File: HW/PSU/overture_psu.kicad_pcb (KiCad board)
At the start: 2 copper layers, 100 x 50 mm, 16 parts, among them J1 OUT, J2 IN, J3 LED

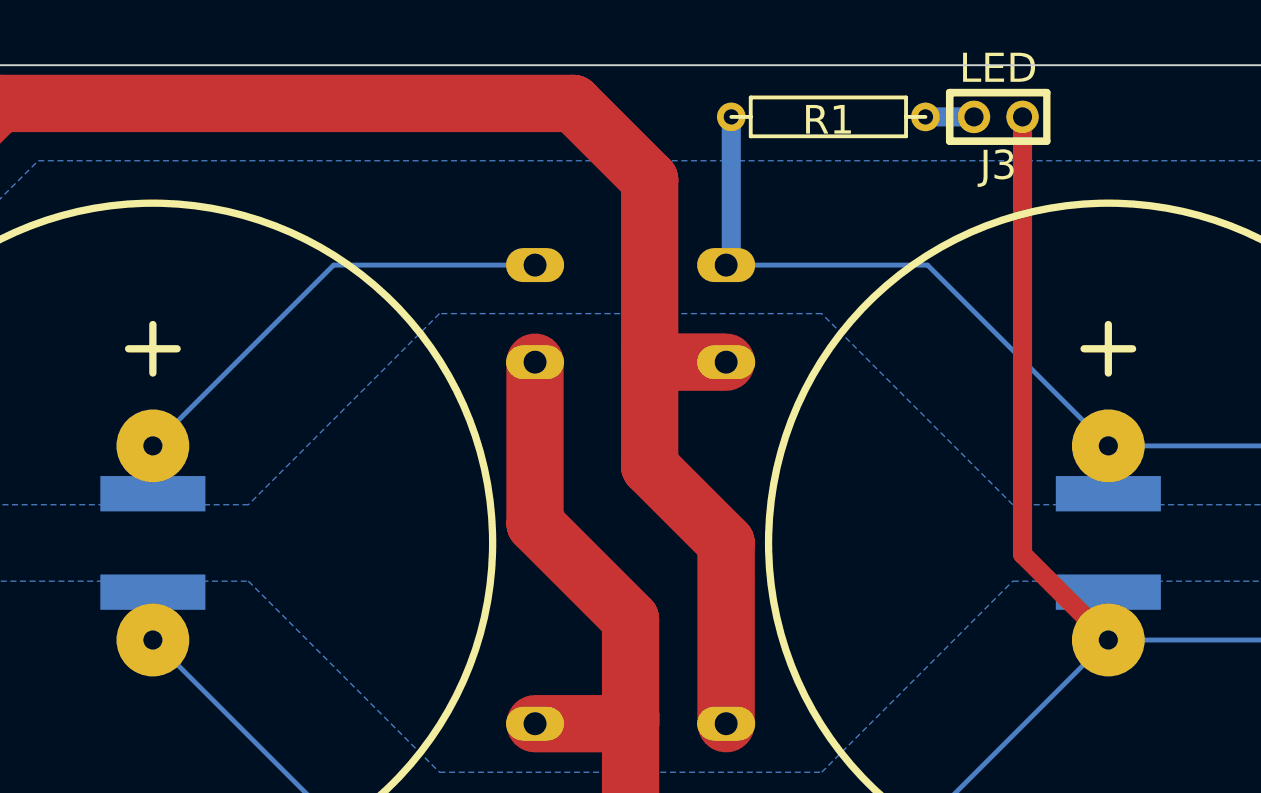
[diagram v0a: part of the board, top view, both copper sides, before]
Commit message: Updated to new KiCAD, Capacitor hole size corrected.
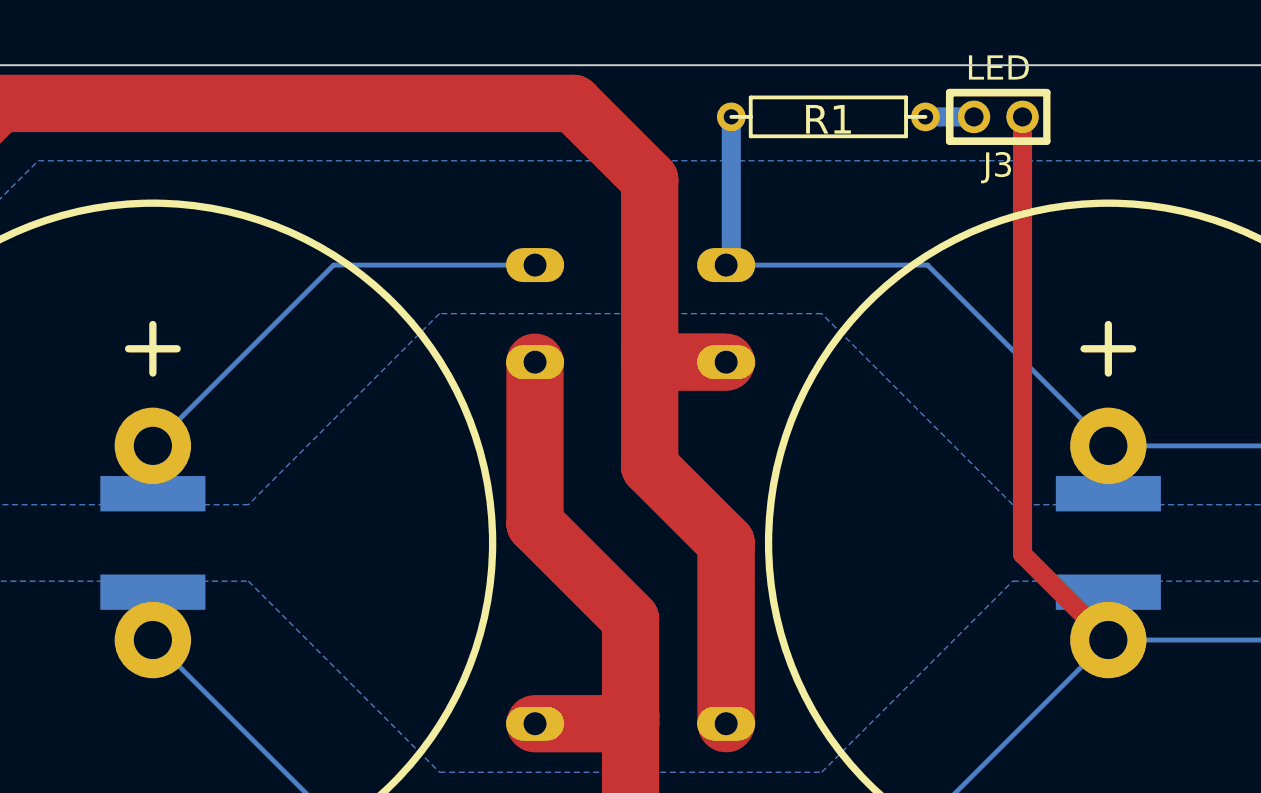
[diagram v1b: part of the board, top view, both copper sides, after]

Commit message: Add V3 (Actually built)
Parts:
- removed MNT_HOLE_3.5 (x4): , MNT_HOLE_3.5
- added C5: 10000uF/50V, Capacitors_ThroughHole:CP_Radial_D35.0mm_P10.00mm_SnapIn, F.Cu at (108.0, 57.0)
- added C6: 10000uF/50V, Capacitors_ThroughHole:CP_Radial_D35.0mm_P10.00mm_SnapIn, F.Cu at (144.0, 57.0)
- added C7: 1uF/250V, Capacitors_ThroughHole:C_Rect_L26.5mm_W11.5mm_P22.50mm_MKS4, F.Cu at (124.5, 32.0)
- added C8: 1uF/250V, Capacitors_ThroughHole:C_Rect_L26.5mm_W11.5mm_P22.50mm_MKS4, F.Cu at (154.5, 32.0)
- added J4: OUT2, suf_connector_ncw:CONN_NCW396-03S, F.Cu at (28.0, 77.0)
- added J5: Protect, Connectors_JST:JST_EH_B03B-EH-A_03x2.50mm_Straight, F.Cu at (150.6, 81.2)
- added MNT_HOLE_3.5S: Val**, suf_mounting:MNT_HOLE_3.5S, F.Cu at (141.0, 96.0)
- added MNT_HOLE_3.5S: Val**, suf_mounting:MNT_HOLE_3.5S, F.Cu at (49.0, 96.0)
- added MNT_HOLE_3.5S: Val**, suf_mounting:MNT_HOLE_3.5S, F.Cu at (165.0, 25.0)
- added MNT_HOLE_3.5S: Val**, suf_mounting:MNT_HOLE_3.5S, F.Cu at (25.0, 25.0)
- added REF**: sink60x100, suf_heatsink:sink60x100, F.Cu at (95.0, 90.0)
- C1: footprint C4P_D14 -> Capacitors_ThroughHole:CP_Radial_D35.0mm_P10.00mm_SnapIn
- C2: value 100nF/50V -> 10000uF/50V; footprint c_2220 -> Capacitors_ThroughHole:CP_Radial_D35.0mm_P10.00mm_SnapIn; moved to F.Cu
- C3: value 100nF/50V -> 1uF/250V; footprint c_2220 -> Capacitors_ThroughHole:C_Rect_L26.5mm_W11.5mm_P22.50mm_MKS4; moved to F.Cu
- C4: value 10000uF/50V -> 1uF/250V; footprint C4P_D14 -> Capacitors_ThroughHole:C_Rect_L26.5mm_W11.5mm_P22.50mm_MKS4
- D1, D2, D3, D4: footprint TO220-2 -> TO_SOT_Packages_THT:TO-220-2_Vertical; moved to F.Cu
- J1: value OUT -> OUT1; footprint CONN_NCW396-02R -> suf_connector_ncw:CONN_NCW396-03S
- J2: footprint CONN_NCW396-02R -> Terminal_Blocks:TerminalBlock_bornier-4_P5.08mm; moved to B.Cu
- J3: footprint HDR-2 -> suf_connector_ncw:CONN_NCW254-02S
- R1: footprint R4 -> Resistors_ThroughHole:R_Axial_DIN0207_L6.3mm_D2.5mm_P10.16mm_Horizontal
- moved C3 223.8 mm to (58.0, 32.0), turned to 180 degrees
- moved J3 207.6 mm to (39.0, 78.0)
- moved C4 199.4 mm to (88.0, 32.0), turned to 180 degrees
- moved R1 195.2 mm to (43.0, 78.0)
- moved C1 186.8 mm to (36.0, 57.0), turned to 0 degrees
- moved D1 162.5 mm to (62.5, 87.0)
- moved D3 157.8 mm to (77.5, 87.0)
- moved C2 157.3 mm to (72.0, 57.0), turned to 0 degrees
- moved J1 130.0 mm to (162.0, 77.0), turned to 0 degrees
- moved D2 126.1 mm to (117.5, 87.0)
- moved D4 122.3 mm to (132.5, 87.0)
- moved J2 104.4 mm to (102.5, 78.0), turned to 180 degrees
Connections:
- C1 pad 1: N-000001 -> Net-(C1-Pad1)
- C1 pad 2: N-000005 -> GND
- C2 pad 1: N-000001 -> GND
- C2 pad 2: N-000005 -> Net-(C2-Pad2)
- C3 pad 1: N-000001 -> GND
- C3 pad 2: N-000005 -> Net-(C1-Pad1)
- C4 pad 1: N-000001 -> Net-(C2-Pad2)
- C4 pad 2: N-000005 -> GND
- D1 pad 1: N-000001 -> Net-(C1-Pad1)
- D2 pad 1: N-000002 -> Net-(D2-Pad1)
- D3 pad 1: N-000001 -> Net-(C1-Pad1)
- D4 pad 1: N-000003 -> Net-(D1-Pad2)
- J1 pad 1: N-000001 -> Net-(C1-Pad1)
- J1 pad 2: N-000005 -> GND
- J2 pad 1: N-000002 -> Net-(D2-Pad1)
- J2 pad 2: N-000003 -> GND
- J3 pad 1: N-000005 -> Net-(J3-Pad1)
- J3 pad 2: N-000004 -> GND
- R1 pad 1: N-000001 -> Net-(J3-Pad1)
- R1 pad 2: N-000004 -> Net-(C1-Pad1)
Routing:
- net GND: track 0.00 -> 326.8 mm
- net Net-(C1-Pad1): track 0.00 -> 299.1 mm
- net Net-(C2-Pad2): track 0.00 -> 281.9 mm
- net N-000005: track 104.4 -> 0.00 mm
- net Net-(D1-Pad2): track 0.00 -> 104.0 mm
- net N-000002: track 98.0 -> 0.00 mm
- net N-000003: track 97.1 -> 0.00 mm
- net N-000001: track 83.0 -> 0.00 mm
- net Net-(D2-Pad1): track 0.00 -> 53.5 mm
- net Net-(J3-Pad1): track 0.00 -> 3.00 mm
- net N-000004: track 2.54 -> 0.00 mm
- added copper zone on B.Cu, net GND
- removed copper zone on B.Cu, net N-000001
- removed copper zone on B.Cu, net N-000005
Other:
- board size 100 x 50 mm -> 150 x 80 mm
- board text added: "Gainclone PSU V3 Design by SUF"
- board text removed: "GainClone PSU - DESIGN BY SUF"
